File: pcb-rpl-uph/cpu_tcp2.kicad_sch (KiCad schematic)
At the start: 1 part, among them U5 RPL_UPH_FCBGA1744

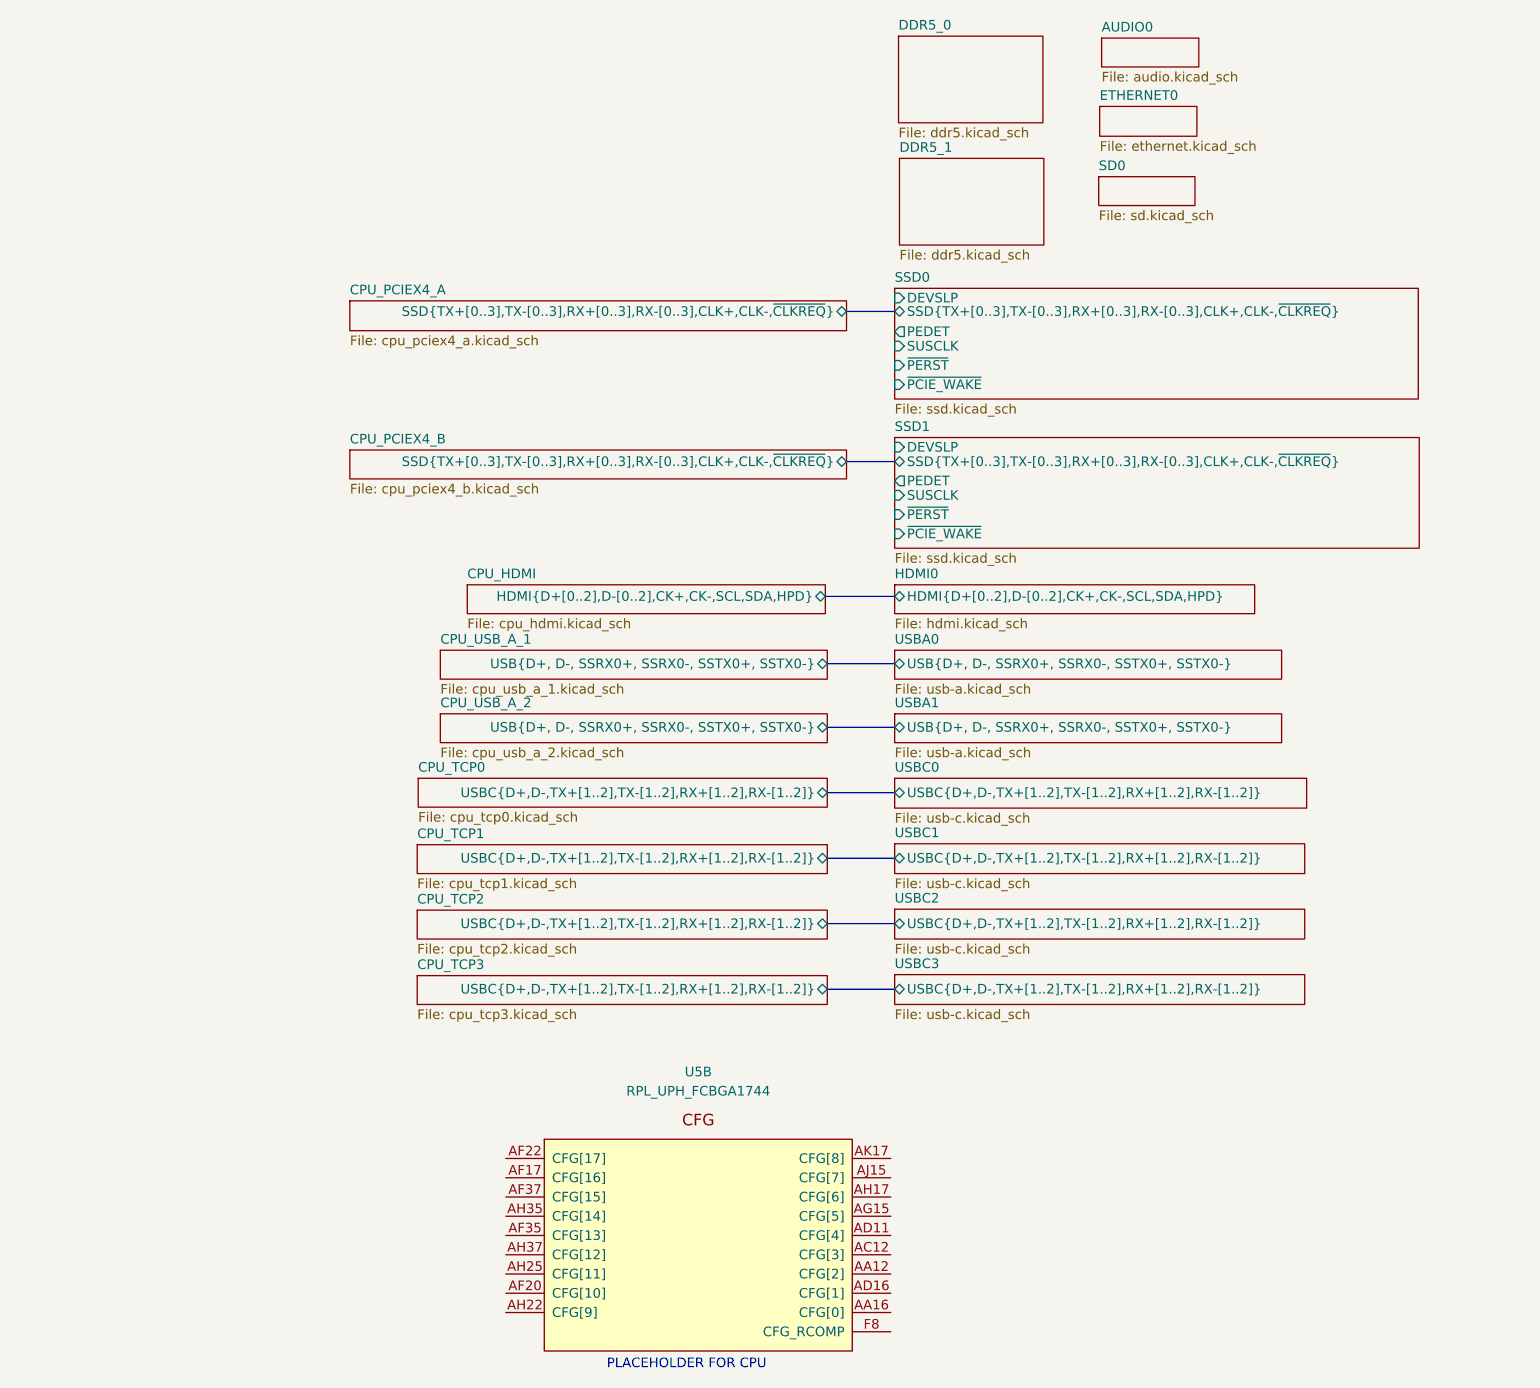
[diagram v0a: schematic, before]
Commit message: Connect USB-A and USB-C data
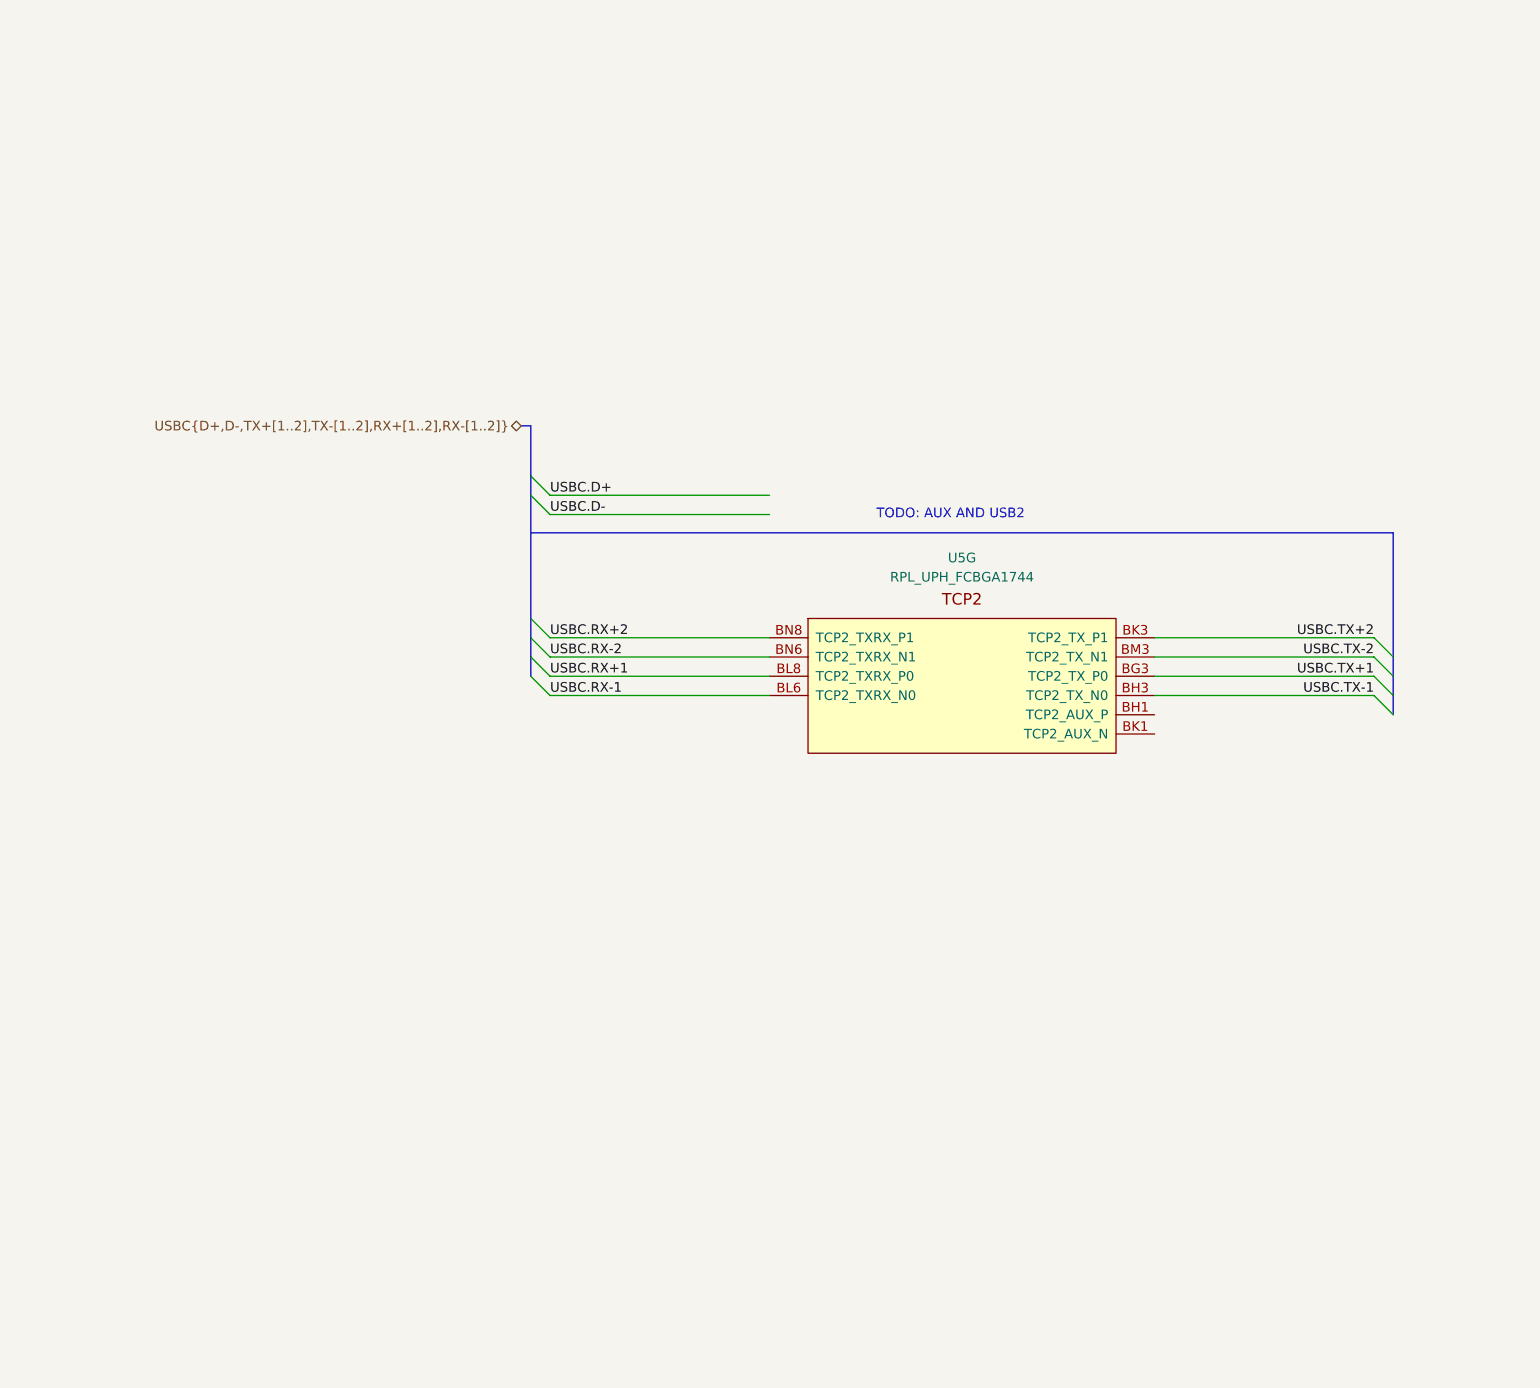
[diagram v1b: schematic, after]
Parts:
- removed U5: RPL_UPH_FCBGA1744, local:RPL_UPH_FCBGA1744, symbol local:RPL_UPH_FCBGA1744
- added U5: RPL_UPH_FCBGA1744, symbol local:RPL_UPH_FCBGA1744
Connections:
- new net USBC.RX+1: U5.BL8 (TCP2_TXRX_P0)
- new net USBC.RX+2: U5.BN8 (TCP2_TXRX_P1)
- new net USBC.RX-1: U5.BL6 (TCP2_TXRX_N0)
- new net USBC.RX-2: U5.BN6 (TCP2_TXRX_N1)
- new net USBC.TX+1: U5.BG3 (TCP2_TX_P0)
- new net USBC.TX+2: U5.BK3 (TCP2_TX_P1)
- new net USBC.TX-1: U5.BH3 (TCP2_TX_N0)
- new net USBC.TX-2: U5.BM3 (TCP2_TX_N1)
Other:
- removed sheet AUDIO0
- removed sheet CPU_HDMI
- removed sheet CPU_PCIEX4_A
- removed sheet CPU_PCIEX4_B
- removed sheet CPU_TCP0
- removed sheet CPU_TCP1
- removed sheet CPU_TCP2
- removed sheet CPU_TCP3
- removed sheet CPU_USB_A_1
- removed sheet CPU_USB_A_2
- removed sheet DDR5_0
- removed sheet DDR5_1
- removed sheet ETHERNET0
- removed sheet HDMI0
- removed sheet SD0
- removed sheet SSD0
- removed sheet SSD1
- removed sheet USBA0
- removed sheet USBA1
- removed sheet USBC0
- removed sheet USBC1
- removed sheet USBC2
- removed sheet USBC3
- note added: "TODO: AUX AND USB2"
- note removed: "PLACEHOLDER FOR CPU"

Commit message: add display connector
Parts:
- U5: footprint (none) -> local:RPL_UPH_FCBGA1744
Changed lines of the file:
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@@
       (effects (font (size 1.27 1.27)))
     )
-    (property "Footprint" "" (at 151.13 89.281 0)
+    (property "Footprint" "local:RPL_UPH_FCBGA1744" (at 151.13 89.281 0)
       (effects (font (size 1.27 1.27)) hide)
     )
